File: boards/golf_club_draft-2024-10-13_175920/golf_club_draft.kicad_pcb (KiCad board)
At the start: 2 copper layers, 1 part

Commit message: Completed first draft of PCB
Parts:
- removed ESP32MC1: ESP32-S3-WROOM-2, RF_Module:ESP32-S3-WROOM-2
- added 1V8LR1: AZ1117-1.8, Package_TO_SOT_SMD:SOT-223-3_TabPin2, F.Cu at (205.1, 82.7)
- added 3V3LR1: AZ1117-3.3, Package_TO_SOT_SMD:SOT-223-3_TabPin2, F.Cu at (192.3, 82.7)
- added BATTCHARGER1: LTC4060EFE, Package_SO:TSSOP-16-1EP_4.4x5mm_P0.65mm, F.Cu at (164.9, 84.6)
- added BATTIO1: Conn_01x03_Socket, Connector_Molex:Molex_KK-254_AE-6410-03A_1x03_P2.54mm_Vertical, F.Cu at (184.5, 93.3)
- added C1: 10uF, Capacitor_SMD:C_0805_2012Metric_Pad1.18x1.45mm_HandSolder, F.Cu at (194.6, 91.0)
- added C10: 0.1uF, Capacitor_SMD:C_0805_2012Metric_Pad1.18x1.45mm_HandSolder, F.Cu at (191.9, 48.9)
- added C11: 0.1uF, Capacitor_SMD:C_0805_2012Metric_Pad1.18x1.45mm_HandSolder, F.Cu at (194.6, 46.9)
- added C2: 22uF, Capacitor_SMD:C_0805_2012Metric_Pad1.18x1.45mm_HandSolder, F.Cu at (196.8, 75.1)
- added C3: 10uF, Capacitor_SMD:C_0805_2012Metric_Pad1.18x1.45mm_HandSolder, F.Cu at (207.4, 91.1)
- added C4: 22uF, Capacitor_SMD:C_0805_2012Metric_Pad1.18x1.45mm_HandSolder, F.Cu at (208.9, 75.1)
- added C5: 1.5nF, Capacitor_SMD:C_0805_2012Metric_Pad1.18x1.45mm_HandSolder, F.Cu at (175.1, 80.4)
- added C6: 0.1uF, Capacitor_SMD:C_0805_2012Metric_Pad1.18x1.45mm_HandSolder, F.Cu at (143.1, 82.2)
- added C7: 1uF, Capacitor_SMD:C_0805_2012Metric_Pad1.18x1.45mm_HandSolder, F.Cu at (147.7, 52.5)
- added C9: 0.1uF, Capacitor_SMD:C_0805_2012Metric_Pad1.18x1.45mm_HandSolder, F.Cu at (197.6, 46.3)
- added D1: LED, LED_SMD:LED_0805_2012Metric_Pad1.15x1.40mm_HandSolder, F.Cu at (154.1, 90.9)
- added D2: D_Schottky, Diode_SMD:D_0805_2012Metric_Pad1.15x1.40mm_HandSolder, F.Cu at (138.6, 87.8)
- added FSR_IO1: Conn_01x04_Socket, Connector_Molex:Molex_KK-254_AE-6410-04A_1x04_P2.54mm_Vertical, F.Cu at (121.2, 64.5)
- added FSR_V1: Conn_01x04_Socket, Connector_Molex:Molex_KK-254_AE-6410-04A_1x04_P2.54mm_Vertical, F.Cu at (121.0, 58.2)
- added IMU_IO1: Conn_01x05_Socket, Connector_Molex:Molex_KK-254_AE-6410-05A_1x05_P2.54mm_Vertical, F.Cu at (211.2, 57.0)
- added J1: USB_C_Receptacle_USB2.0_16P, Connector_USB:USB_C_Receptacle_HRO_TYPE-C-31-M-12, F.Cu at (125.3, 90.3)
- added Q1: PNP, Connector_PinSocket_1.27mm:PinSocket_1x03_P1.27mm_Vertical, F.Cu at (175.1, 86.2)
- added Q2: NPN, Connector_PinSocket_1.27mm:PinSocket_1x03_P1.27mm_Vertical, F.Cu at (139.8, 69.3)
- added Q3: PNP, Connector_PinSocket_1.27mm:PinSocket_1x03_P1.27mm_Vertical, F.Cu at (143.6, 65.4)
- added R1: 330, Resistor_SMD:R_0805_2012Metric_Pad1.20x1.40mm_HandSolder, F.Cu at (146.6, 90.9)
- added R3: 698, Resistor_SMD:R_0805_2012Metric_Pad1.20x1.40mm_HandSolder, F.Cu at (169.0, 75.6)
- added R4: 5.1k, Resistor_SMD:R_0805_2012Metric_Pad1.20x1.40mm_HandSolder, F.Cu at (135.3, 90.6)
- added R5: 5.1k, Resistor_SMD:R_0805_2012Metric_Pad1.20x1.40mm_HandSolder, F.Cu at (135.3, 92.8)
- added R6: 10K, Resistor_SMD:R_0805_2012Metric_Pad1.20x1.40mm_HandSolder, F.Cu at (127.1, 63.5)
- added R7: 10K, Resistor_SMD:R_0805_2012Metric_Pad1.20x1.40mm_HandSolder, F.Cu at (127.9, 66.9)
- added R8: 10K, Resistor_SMD:R_0805_2012Metric_Pad1.20x1.40mm_HandSolder, F.Cu at (132.7, 69.6)
- added R9: 10K, Resistor_SMD:R_0805_2012Metric_Pad1.20x1.40mm_HandSolder, F.Cu at (135.3, 73.2)
- added U1: ICM-20948, Sensor_Motion:InvenSense_QFN-24_3x3mm_P0.4mm, F.Cu at (194.8, 53.2)
- added U2: CP2104, Package_DFN_QFN:QFN-24-1EP_4x4mm_P0.5mm_EP2.6x2.6mm, F.Cu at (138.0, 78.0)
- added U3: ESP32-S3-WROOM-1, RF_Module:ESP32-S3-WROOM-1, F.Cu at (166.1, 54.2)
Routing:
- net /3V3: track 0.00 -> 188.8 mm, vias 0 -> 4
- net /VIN: track 0.00 -> 76.0 mm
- net /RXD: track 0.00 -> 69.0 mm, vias 0 -> 2
- net /TXD: track 0.00 -> 65.9 mm
- net /1V8: track 0.00 -> 62.4 mm
- net /SDA: track 0.00 -> 58.9 mm, vias 0 -> 4
- net /SCL: track 0.00 -> 56.4 mm, vias 0 -> 4
- net GND: track 0.00 -> 56.4 mm, vias 0 -> 17
- net /VBATT: track 0.00 -> 55.2 mm
- net /FSR4: track 0.00 -> 46.3 mm
- net /FSR3: track 0.00 -> 44.7 mm
- net /FSR2: track 0.00 -> 41.6 mm
- net /FSR1: track 0.00 -> 41.1 mm
- net /GPIO0: track 0.00 -> 37.1 mm, vias 0 -> 3
- net /RESET: track 0.00 -> 29.5 mm, vias 0 -> 2
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- added copper zone on F.Cu, net GND
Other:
- board outline added: 97.8 x 57 mm
- board text added: "Positional Golf Sensors V1 10/21/2024 Team 15"

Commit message: 3rd round PCB order revisions
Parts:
- removed C10, C11, C9: 0.1uF, Capacitor_SMD:C_0805_2012Metric_Pad1.18x1.45mm_HandSolder
- removed U1: ICM-20948, Sensor_Motion:InvenSense_QFN-24_3x3mm_P0.4mm
- added H1: MountingHole, MountingHole:MountingHole_3.2mm_M3, F.Cu at (53.7, 50.8)
- added H2: MountingHole, MountingHole:MountingHole_3.2mm_M3, F.Cu at (129.9, 50.8)
- added R10: 10K, Resistor_SMD:R_0805_2012Metric_Pad1.20x1.40mm_HandSolder, F.Cu at (99.0, 47.8)
- added R11: 10K, Resistor_SMD:R_0805_2012Metric_Pad1.20x1.40mm_HandSolder, F.Cu at (63.9, 45.0)
- added R12: 10K, Resistor_SMD:R_0805_2012Metric_Pad1.20x1.40mm_HandSolder, F.Cu at (90.0, 49.0)
- added R2: 10K, Resistor_SMD:R_0805_2012Metric_Pad1.20x1.40mm_HandSolder, F.Cu at (105.1, 45.0)
- moved IMU_IO1 139.2 mm to (72.0, 61.4), turned to 0 degrees
- moved C4 92.6 mm to (119.6, 50.6), turned to 90 degrees
- moved U3 90.4 mm to (77.2, 37.8)
- moved C3 88.8 mm to (121.9, 66.8)
- moved 1V8LR1 88.8 mm to (119.6, 58.7)
- moved C1 88.2 mm to (109.8, 66.8)
- moved 3V3LR1 88.1 mm to (107.5, 58.7)
- moved C7 87.3 mm to (61.2, 40.9), turned to 90 degrees
- moved R9 85.9 mm to (54.7, 43.3), turned to 180 degrees
- moved C2 85.7 mm to (113.4, 55.4)
- moved R8 84.5 mm to (53.8, 39.4)
- moved FSR_IO1 81.4 mm to (46.0, 33.2)
- moved R7 80.8 mm to (53.2, 36.0)
- moved R6 77.4 mm to (55.9, 33.2), turned to 180 degrees
- moved FSR_V1 75.1 mm to (46.0, 60.4), turned to -90 degrees
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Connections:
- J1 pad S1: unconnected-(J1-SHIELD-PadS1) -> GND
- Q2 pad 1: /RESET -> Net-(Q2-C)
- Q2 pad 2: /DTR -> Net-(Q2-B)
- Q3 pad 1: /GPIO0 -> Net-(Q3-C)
- Q3 pad 2: /RTS -> Net-(Q3-B)
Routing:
- net /RXD: track 69.0 -> 21.0 mm
- net /SDA: track 58.9 -> 11.4 mm, vias 4 -> 0
- net GND: track 56.4 -> 103.7 mm, vias 17 -> 19
- net /SCL: track 56.4 -> 11.4 mm, vias 4 -> 0
- net /TXD: track 65.9 -> 22.5 mm, vias 0 -> 2
- net Net-(Q2-C): track 0.00 -> 42.3 mm, vias 0 -> 2
- net /GPIO0: track 37.1 -> 3.11 mm, vias 3 -> 0
- net /FSR4: track 46.3 -> 24.7 mm, vias 0 -> 2
- net /FSR3: track 44.7 -> 24.6 mm, vias 0 -> 2
- net /3V3: track 188.8 -> 169.6 mm, vias 4 -> 0
- net /FSR2: track 41.6 -> 23.2 mm, vias 0 -> 2
- net /FSR1: track 41.1 -> 23.7 mm, vias 0 -> 2
- net unconnected-(J1-SHIELD-PadS1): track 17.0 -> 0.00 mm
- net /VIN: track 76.0 -> 59.0 mm
- net /1V8: track 62.4 -> 52.0 mm
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- added copper zone on B.Cu, net GND
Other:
- board size 97.8 x 57 mm -> 99 x 39.3 mm
- board text added: "Positional Golf Sensors V2 10/29/2024 Team 15"
- board text removed: "Positional Golf Sensors V1 10/21/2024 Team 15"

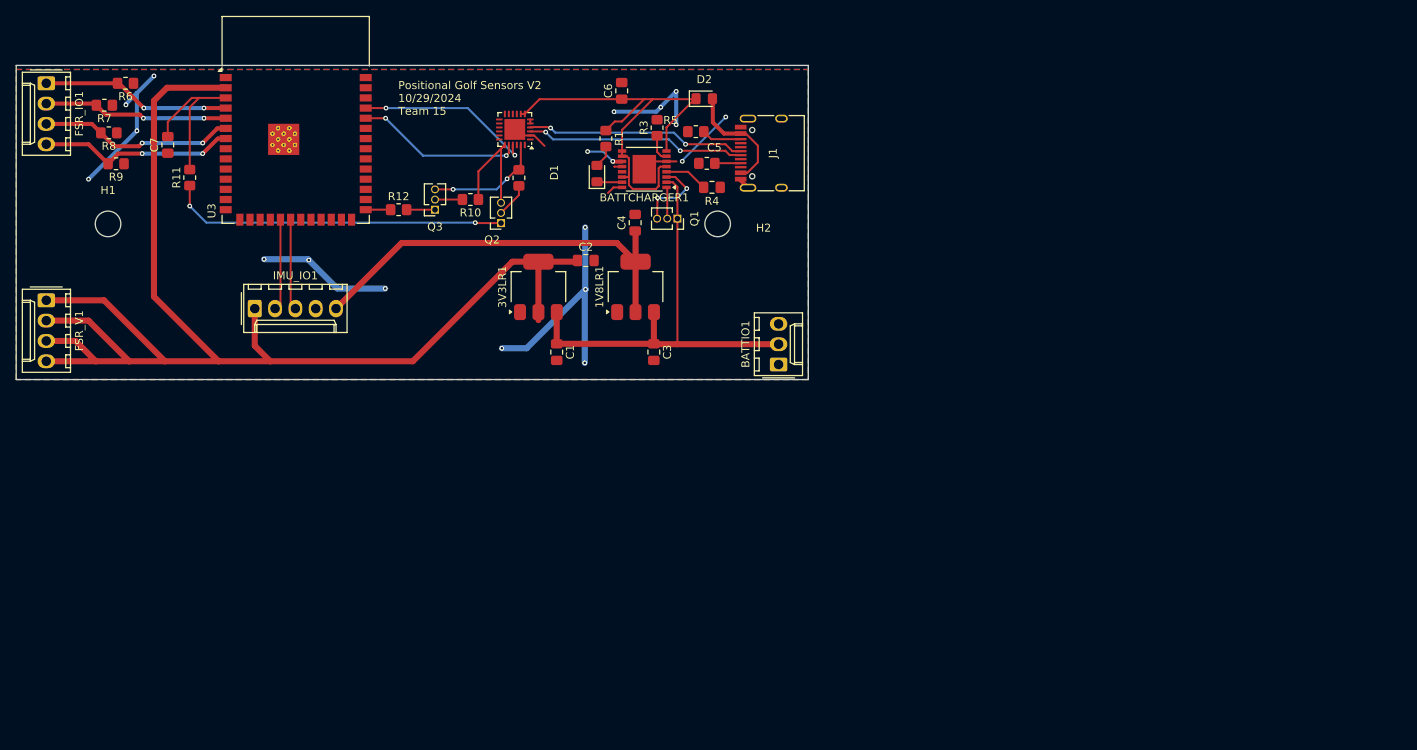
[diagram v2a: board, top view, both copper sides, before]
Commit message: Some more kicad files, round 3 and 4
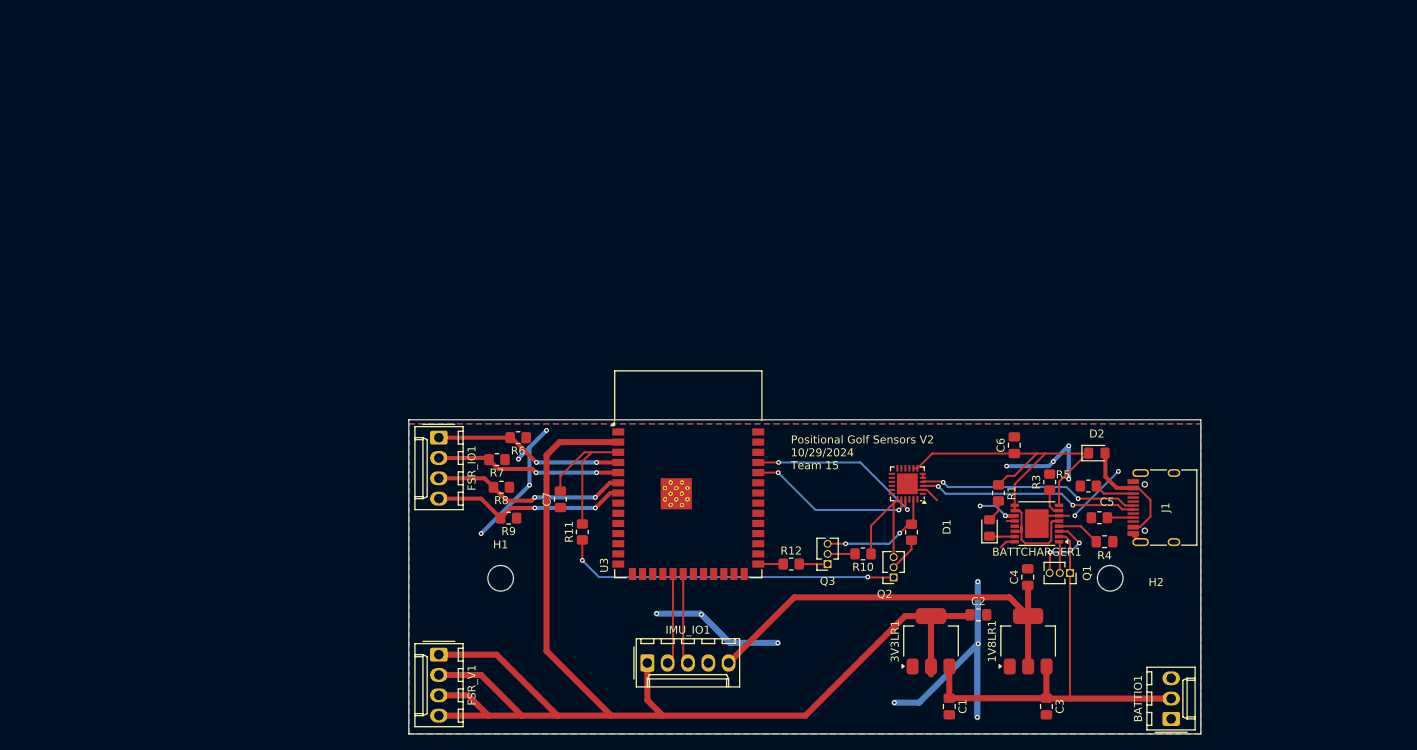
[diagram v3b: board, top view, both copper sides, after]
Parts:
- moved BATTCHARGER1 66.1 mm to (169.8, 88.3)
- moved BATTIO1 66.1 mm to (186.6, 112.7)
- moved C4 66.1 mm to (168.7, 94.9)
- moved C6 66.1 mm to (167.0, 78.5)
- moved C7 66.1 mm to (110.2, 85.2)
- moved D2 66.1 mm to (177.3, 79.5)
- moved H1 66.1 mm to (102.8, 95.1)
- moved H2 66.1 mm to (179.0, 95.1)
- moved J1 66.1 mm to (185.9, 86.3)
- moved Q1 66.1 mm to (173.9, 94.4)
- moved Q3 66.1 mm to (143.6, 93.3)
- moved R4 66.1 mm to (177.6, 87.5)
- moved R9 66.1 mm to (103.8, 87.6)
- moved U2 66.1 mm to (153.6, 83.3)
- moved C1 66.1 mm to (158.9, 111.1)
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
